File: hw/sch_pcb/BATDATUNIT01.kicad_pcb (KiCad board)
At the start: 2 copper layers, 136.2 x 85.9 mm, 222 parts, among them J1 USBC_USB4105-GF-A, J2 SD_Card-FPS009-4200-0, J3 HEADER_2x03, J4 46436-9327, Q1 BC817-25, Q2 BC817-25, Q3 BC817-25, Q4 BC817-25, Q5 BC817-25, Q6 BC817-25, Q7 BSS83P, SW1 SKRTLAE010, SW2 KMT031, SW3 SKRTLAE010, SW4 KMT031, U1 MAX14502AETL+, U10 PCF85263A, U11 TCA4307, U12 BQ34Z100, U13 BQ25628E, U14 SN74HC164P, U15 TPS631000DRLR, U16 TPS631000DRLR, U17 TPS631000DRLR, U18 TPS22965-Q1, U2 USBLC6-2SC6, U4 PCA9541ABS/01, U5 AT24CS64-SSHM, U6 SHT35-DIS, U7 TMUX1574DYYR, U8 ATMEGA1284P-AU, U9 MS561101BA03-50, Y1 19.2 MHz, Y2 8 MHz, Y3 ABS07-120-32.768KHZ-T

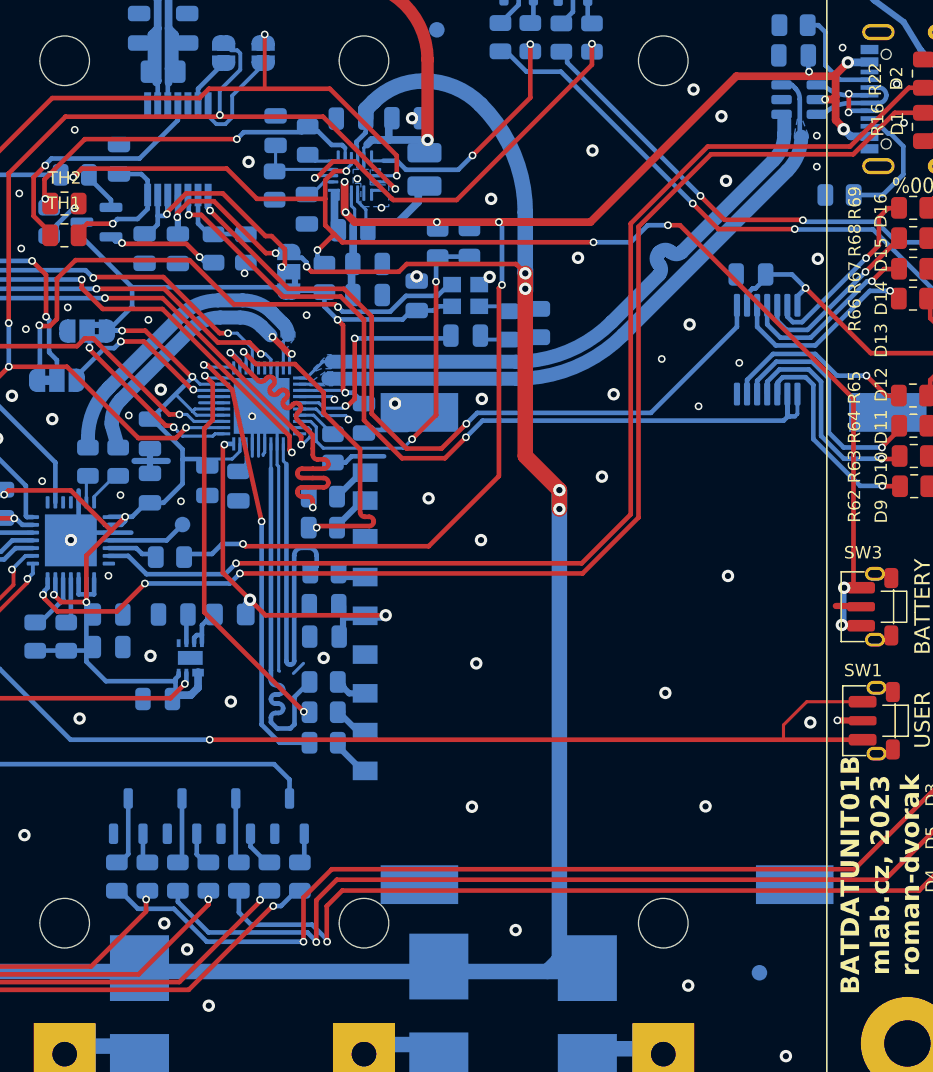
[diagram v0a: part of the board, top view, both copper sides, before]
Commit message: Move SD card reader  oscillator away from USB data tracks and isolate it by GND strip.
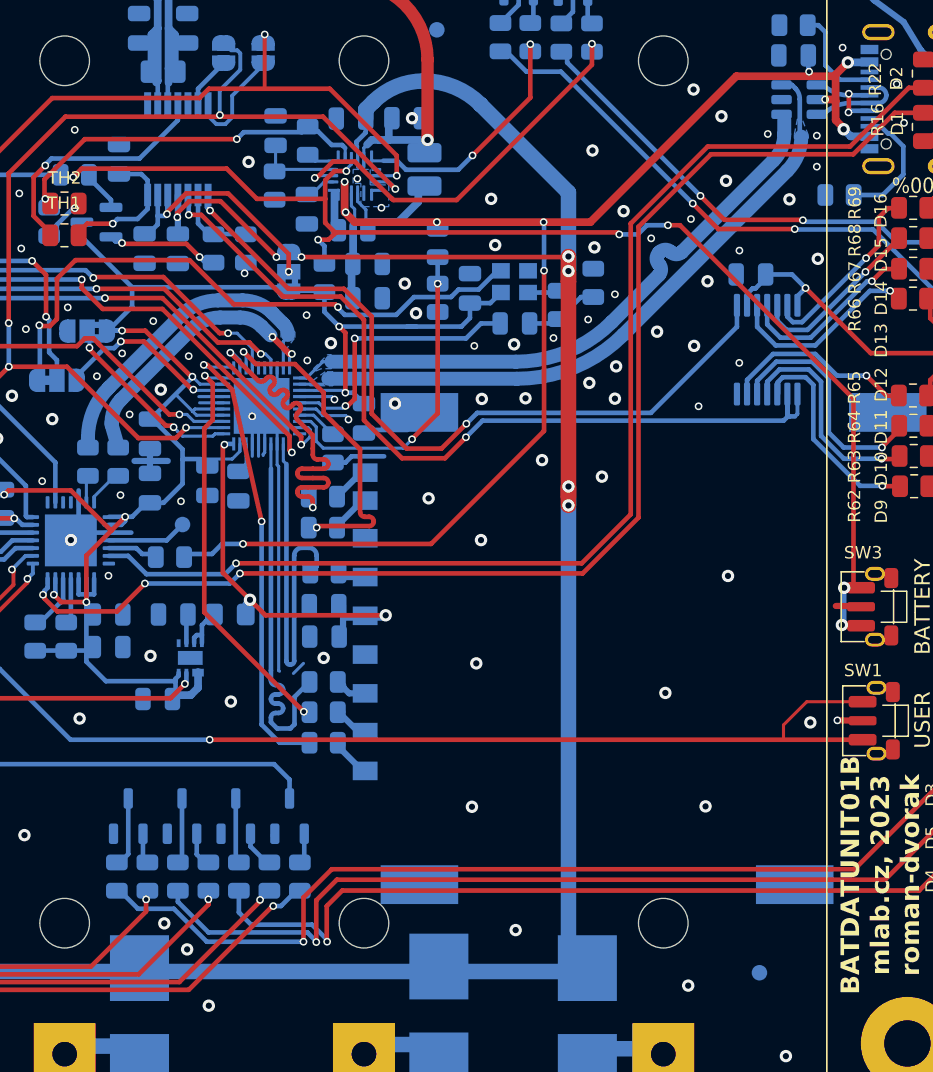
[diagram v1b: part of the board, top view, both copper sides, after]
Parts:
- moved R4 4.34 mm to (194.3, 91.5)
- moved R14 4.11 mm to (184.3, 92.5), turned to -90 degrees
- moved R3 3.49 mm to (192.0, 92.9)
- moved C4 3.47 mm to (186.3, 91.9)
- moved Y1 3.27 mm to (189.2, 91.4)
- moved C49 3.27 mm to (189.2, 94.1)
- moved C23 0.21 mm to (179.7, 92.5)
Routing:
- net +3.3V: track 564.6 -> 569.3 mm
- net /FREF: track 14.1 -> 17.6 mm
- net /mode_osc: track 36.1 -> 39.4 mm
- net +BATT: track 242.6 -> 245.4 mm
- net Net-(U1-KVBUS): track 23.2 -> 21.2 mm
- net VBUS: track 91.5 -> 90.1 mm
- net Net-(C49-Pad1): track 3.97 -> 4.81 mm
- net GND: vias 169 -> 191

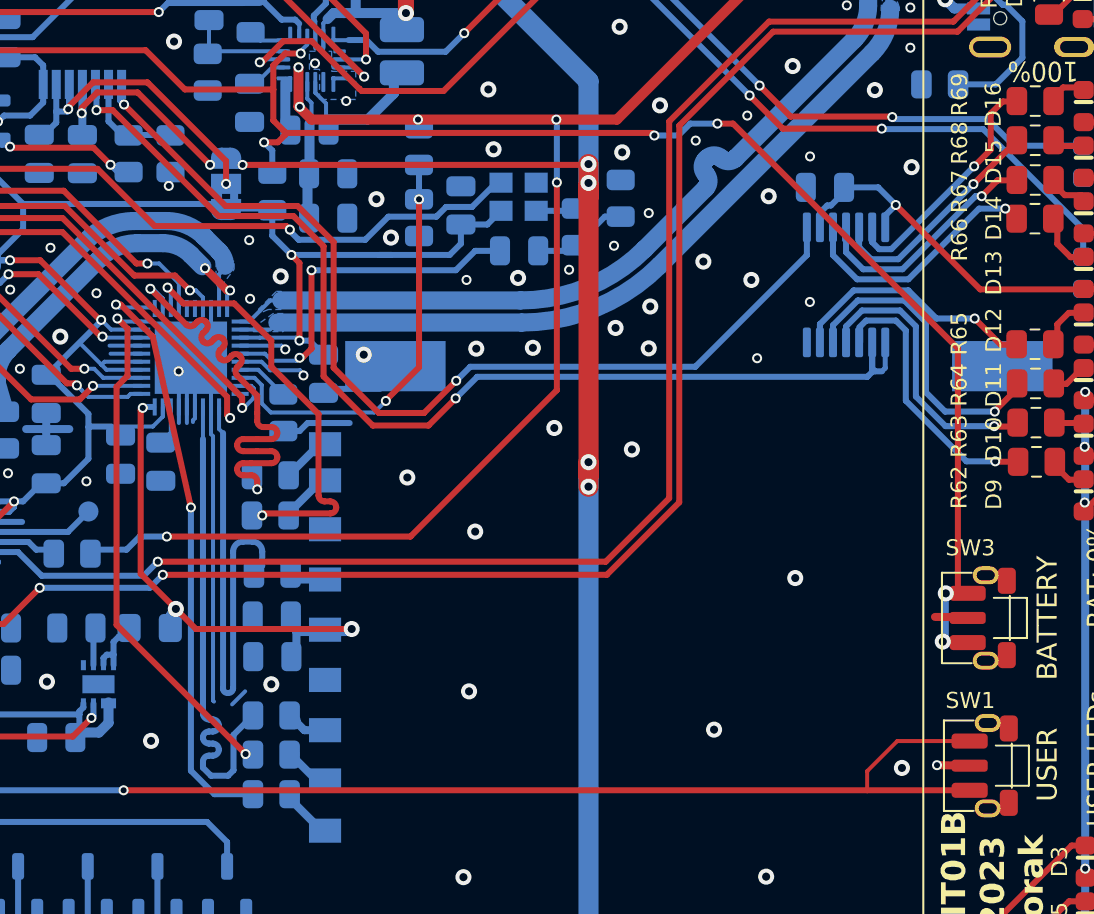
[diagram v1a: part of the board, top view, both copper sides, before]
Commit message: Swap button pins. Resolve #7
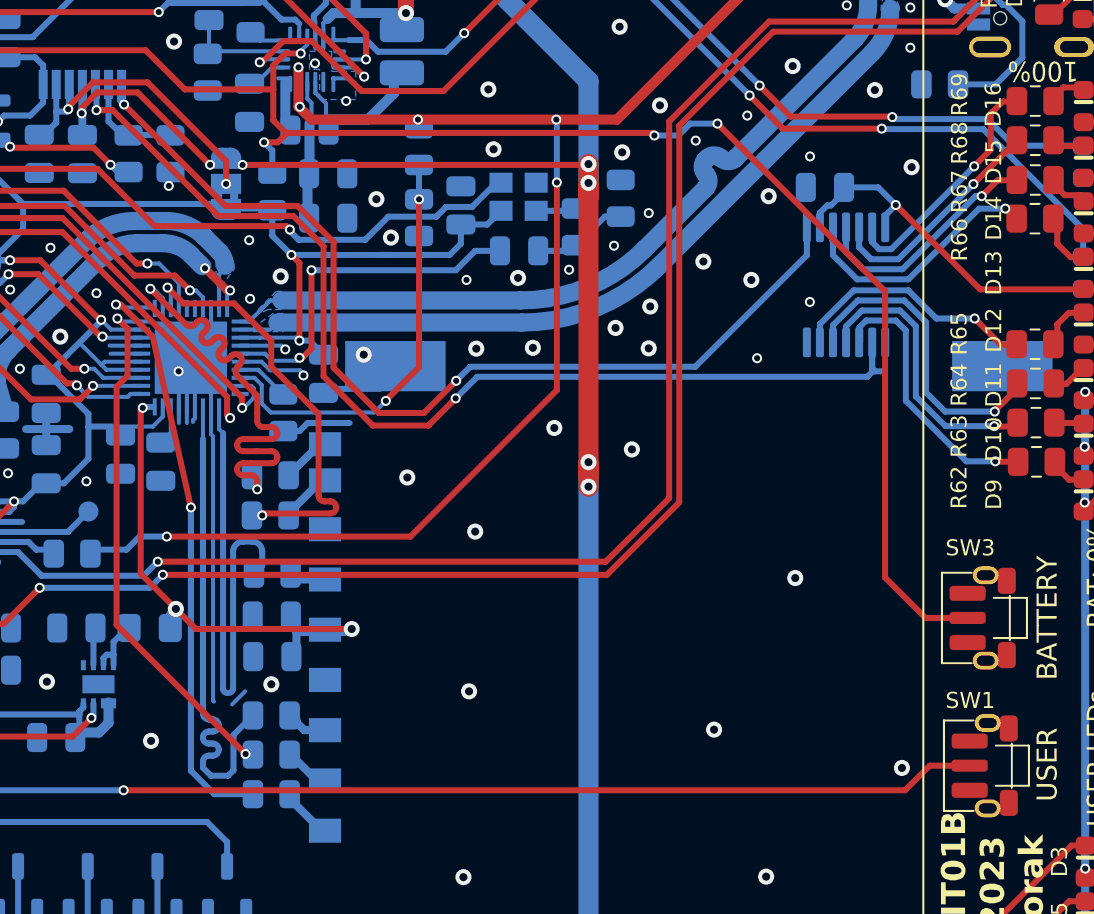
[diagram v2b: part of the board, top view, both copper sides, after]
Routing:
- net /BTN_USER_A: track 119.1 -> 113.0 mm
- net GND: track 94.3 -> 91.1 mm, vias 191 -> 190
- net EXT_DETECTION_CHARGER: track 178.4 -> 176.1 mm, vias 9 -> 7
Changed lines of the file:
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@@
     (fp_line (start 2.25 -1.28) (end 2.25 0.2)
       (stroke (width 0.1) (type default)) (layer "F.SilkS"))
-    (pad "1" smd roundrect (at -1.225 0 90) (size 0.75 1.8) (layers "F.Cu" "F.Paste" "F.Mask") (roundrect_rratio 0.25)
+    (pad "1" smd roundrect (at 0 0 90) (size 0.6 1.8) (layers "F.Cu" "F.Paste" "F.Mask") (roundrect_rratio 0.25)
       (net 210 "EXT_DETECTION_CHARGER") (pinfunction "1") (pintype "passive") (thermal_bridge_angle 45))
-    (pad "1" smd roundrect (at 1.225 0 90) (size 0.75 1.8) (layers "F.Cu" "F.Paste" "F.Mask") (roundrect_rratio 0.25)
-      (net 210 "EXT_DETECTION_CHARGER") (pinfunction "1") (pintype "passive") (thermal_bridge_angle 45))
-    (pad "2" smd roundrect (at 0 0 90) (size 0.6 1.8) (layers "F.Cu" "F.Paste" "F.Mask") (roundrect_rratio 0.25)
+    (pad "2" smd roundrect (at -1.225 0 90) (size 0.75 1.8) (layers "F.Cu" "F.Paste" "F.Mask") (roundrect_rratio 0.25)
+      (net 1 "GND") (pinfunction "2") (pintype "passive") (thermal_bridge_angle 45))
+    (pad "2" smd roundrect (at 1.225 0 90) (size 0.75 1.8) (layers "F.Cu" "F.Paste" "F.Mask") (roundrect_rratio 0.25)
       (net 1 "GND") (pinfunction "2") (pintype "passive") (thermal_bridge_angle 45))
     (pad "GND" thru_hole oval (at -2.125 0.9 90) (size 0.9 1.3) (drill oval 0.5 0.9) (layers "*.Cu" "*.Mask")
@@
     (fp_line (start 2.25 -1.28) (end 2.25 0.2)
       (stroke (width 0.1) (type default)) (layer "F.SilkS"))
-    (pad "1" smd roundrect (at -1.225 0 90) (size 0.75 1.8) (layers "F.Cu" "F.Paste" "F.Mask") (roundrect_rratio 0.25)
+    (pad "1" smd roundrect (at 0 0 90) (size 0.6 1.8) (layers "F.Cu" "F.Paste" "F.Mask") (roundrect_rratio 0.25)
       (net 43 "/BTN_USER_A") (pinfunction "1") (pintype "passive") (thermal_bridge_angle 45))
-    (pad "1" smd roundrect (at 1.225 0 90) (size 0.75 1.8) (layers "F.Cu" "F.Paste" "F.Mask") (roundrect_rratio 0.25)
-      (net 43 "/BTN_USER_A") (pinfunction "1") (pintype "passive") (thermal_bridge_angle 45))
-    (pad "2" smd roundrect (at 0 0 90) (size 0.6 1.8) (layers "F.Cu" "F.Paste" "F.Mask") (roundrect_rratio 0.25)
+    (pad "2" smd roundrect (at -1.225 0 90) (size 0.75 1.8) (layers "F.Cu" "F.Paste" "F.Mask") (roundrect_rratio 0.25)
+      (net 1 "GND") (pinfunction "2") (pintype "passive") (thermal_bridge_angle 45))
+    (pad "2" smd roundrect (at 1.225 0 90) (size 0.75 1.8) (layers "F.Cu" "F.Paste" "F.Mask") (roundrect_rratio 0.25)
       (net 1 "GND") (pinfunction "2") (pintype "passive") (thermal_bridge_angle 45))
     (pad "GND" thru_hole oval (at -2.125 0.9 90) (size 0.9 1.3) (drill oval 0.5 0.9) (layers "*.Cu" "*.Mask")
@@
     (style (thickness 0.15) (arrow_length 1.27) (text_position_mode 0) (extension_height 0.58642) (extension_offset 0.5) keep_text_aligned)
   )
-  (segment (start 210.025 119.725) (end 210.05 119.75) (width 0.4) (layer "F.Cu") (net 1))
+  (segment (start 211.516 113.576) (end 211.565 113.625) (width 0.3) (layer "F.Cu") (net 1))
   (segment (start 98.15 102) (end 95 102) (width 0.4) (layer "F.Cu") (net 1))
-  (segment (start 211.65 119.75) (end 210.025 119.725) (width 0.4) (layer "F.Cu") (net 1))
-  (segment (start 211.515 112.35) (end 209.925 112.35) (width 0.4) (layer "F.Cu") (net 1))
   (via (at 144.4498 73.4822) (size 0.8) (drill 0.4) (layers "F.Cu" "B.Cu") (free) (net 1))
   (via (at 141.859 78.1558) (size 0.8) (drill 0.4) (layers "F.Cu" "B.Cu") (free) (net 1))
@@
   (via (at 201.6506 91.4146) (size 0.8) (drill 0.4) (layers "F.Cu" "B.Cu") (free) (net 1))
   (via (at 143.2052 79.2988) (size 0.8) (drill 0.4) (layers "F.Cu" "B.Cu") (free) (net 1))
-  (via (at 210.025 119.725) (size 0.5) (drill 0.3) (layers "F.Cu" "B.Cu") (net 1))
   (via (at 115.25 96) (size 0.5) (drill 0.3) (layers "F.Cu" "B.Cu") (free) (net 1))
   (via (at 169.4942 138.1252) (size 0.8) (drill 0.4) (layers "F.Cu" "B.Cu") (free) (net 1))
@@
   (segment (start 112.35 77.62) (end 112.55 77.62) (width 0.3) (layer "B.Cu") (net 42))
   (segment (start 117.563589 98.511411) (end 117.563589 99.456411) (width 0.3) (layer "B.Cu") (net 42))
-  (segment (start 211.65 118.525) (end 208.05 118.525) (width 0.2) (layer "F.Cu") (net 43))
+  (segment (start 211.65 119.75) (end 209.6626 119.75) (width 0.3) (layer "F.Cu") (net 43))
   (segment (start 116.6 104.9) (end 116.6 105.6) (width 0.3) (layer "F.Cu") (net 43))
-  (segment (start 211.65 120.975) (end 206.55 120.975) (width 0.3) (layer "F.Cu") (net 43))
   (segment (start 125.348529 108.5) (end 133.248529 116.4) (width 0.3) (layer "F.Cu") (net 43))
-  (segment (start 206.55 120.975) (end 169.55 120.975) (width 0.3) (layer "F.Cu") (net 43))
+  (segment (start 209.6626 119.75) (end 208.4376 120.975) (width 0.3) (layer "F.Cu") (net 43))
   (segment (start 119.5 108.5) (end 125.348529 108.5) (width 0.3) (layer "F.Cu") (net 43))
   (segment (start 116.6 105.6) (end 119.5 108.5) (width 0.3) (layer "F.Cu") (net 43))
-  (segment (start 206.55 120.025) (end 206.55 120.975) (width 0.2) (layer "F.Cu") (net 43))
   (segment (start 133.248529 116.4) (end 143.9 116.4) (width 0.3) (layer "F.Cu") (net 43))
-  (segment (start 208.05 118.525) (end 206.55 120.025) (width 0.2) (layer "F.Cu") (net 43))
+  (segment (start 208.4376 120.975) (end 169.55 120.975) (width 0.3) (layer "F.Cu") (net 43))
   (via (at 143.9 116.4) (size 0.5) (drill 0.3) (layers "F.Cu" "B.Cu") (net 43))
   (via (at 169.55 120.975) (size 0.5) (drill 0.3) (layers "F.Cu" "B.Cu") (net 43))
@@
   (segment (start 118.419341 124.312893) (end 117.666117 125.066117) (width 0.25) (layer "B.Cu") (net 207))
   (arc (start 119.126448 124.02) (mid 118.743765 124.09612) (end 118.419341 124.312893) (width 0.25) (layer "B.Cu") (net 207))
-  (segment (start 210.465 111.175) (end 210.464 111.176) (width 0.3) (layer "F.Cu") (net 210))
+  (segment (start 207.4418 96.1418) (end 207.4418 110.3884) (width 0.3) (layer "F.Cu") (net 210))
   (segment (start 195.834 88.265) (end 195.961 88.392) (width 0.3) (layer "F.Cu") (net 210))
   (segment (start 146.3 119.9) (end 146.3 112.9) (width 0.3) (layer "F.Cu") (net 210))
   (segment (start 146.3 112.9) (end 142.9 109.5) (width 0.3) (layer "F.Cu") (net 210))
   (segment (start 160.75 84.7) (end 161.3 84.15) (width 0.3) (layer "F.Cu") (net 210))
-  (segment (start 211.516 113.576) (end 211.565 113.625) (width 0.3) (layer "F.Cu") (net 210))
-  (segment (start 211.064 98.989) (end 211.064 110.926) (width 0.3) (layer "F.Cu") (net 210))
   (segment (start 177 87.6428) (end 177 86.1) (width 0.3) (layer "F.Cu") (net 210))
   (segment (start 177.575 88.375) (end 177.2182 88.7318) (width 0.3) (layer "F.Cu") (net 210))
   (segment (start 177.685 88.265) (end 195.834 88.265) (width 0.3) (layer "F.Cu") (net 210))
   (segment (start 177 84.9) (end 177 86.1) (width 0.3) (layer "F.Cu") (net 210))
-  (segment (start 210.314 113.576) (end 211.516 113.576) (width 0.3) (layer "F.Cu") (net 210))
+  (segment (start 207.4418 110.3884) (end 209.4534 112.4) (width 0.3) (layer "F.Cu") (net 210))
+  (segment (start 199.1 87.8) (end 207.4418 96.1418) (width 0.3) (layer "F.Cu") (net 210))
   (segment (start 177.589471 84.310529) (end 177 84.9) (width 0.3) (layer "F.Cu") (net 210))
   (segment (start 142.9 109.5) (end 142.9 102.848529) (width 0.3) (layer "F.Cu") (net 210))
-  (segment (start 199.1 87.8) (end 199.875 87.8) (width 0.3) (layer "F.Cu") (net 210))
   (segment (start 178.364466 84.310529) (end 177.589471 84.310529) (width 0.3) (layer "F.Cu") (net 210))
   (segment (start 161.3 84.15) (end 170.65 84.15) (width 0.3) (layer "F.Cu") (net 210))
@@
   (segment (start 177.2182 88.7318) (end 176.541565 88.7318) (width 0.3) (layer "F.Cu") (net 210))
   (segment (start 170.65 84.15) (end 172.6 86.1) (width 0.3) (layer "F.Cu") (net 210))
-  (segment (start 199.875 87.8) (end 211.064 98.989) (width 0.3) (layer "F.Cu") (net 210))
-  (segment (start 211.565 111.175) (end 210.465 111.175) (width 0.3) (layer "F.Cu") (net 210))
+  (segment (start 209.4534 112.4) (end 211.55 112.4) (width 0.3) (layer "F.Cu") (net 210))
   (segment (start 177.575 88.375) (end 177.575 88.2178) (width 0.3) (layer "F.Cu") (net 210))
   (segment (start 172.6 86.1) (end 177 86.1) (width 0.3) (layer "F.Cu") (net 210))
@@
   (via (at 178.364466 84.310529) (size 0.5) (drill 0.3) (layers "F.Cu" "B.Cu") (net 210))
   (via (at 195.961 88.392) (size 0.5) (drill 0.3) (layers "F.Cu" "B.Cu") (net 210))
-  (via (at 210.464 111.176) (size 0.8) (drill 0.4) (layers "F.Cu" "B.Cu") (net 210))
   (via (at 199.1 87.8) (size 0.5) (drill 0.3) (layers "F.Cu" "B.Cu") (net 210))
-  (via (at 210.314 113.576) (size 0.8) (drill 0.4) (layers "F.Cu" "B.Cu") (net 210))
   (via (at 153.299996 84.55) (size 0.5) (drill 0.3) (layers "F.Cu" "B.Cu") (net 210))
   (segment (start 197.7468 87.8) (end 197.1548 88.392) (width 0.3) (layer "B.Cu") (net 210))
@@
   (segment (start 153.3 84.55) (end 153.299996 84.55) (width 0.3) (layer "B.Cu") (net 210))
   (segment (start 140.5 125.7) (end 146.3 119.9) (width 0.3) (layer "B.Cu") (net 210))
-  (segment (start 210.464 111.176) (end 210.464 113.426) (width 0.3) (layer "B.Cu") (net 210))
   (segment (start 116.6 87.41) (end 116.6 85.4375) (width 0.3) (layer "B.Cu") (net 210))
   (segment (start 197.1548 88.392) (end 195.961 88.392) (width 0.3) (layer "B.Cu") (net 210))
@@
   (segment (start 176.95 89.140235) (end 176.541565 88.7318) (width 0.3) (layer "B.Cu") (net 210))
   (segment (start 116.6 87.41) (end 117.06 86.95) (width 0.3) (layer "B.Cu") (net 210))
-  (segment (start 210.464 113.426) (end 210.314 113.576) (width 0.3) (layer "B.Cu") (net 210))
   (segment (start 148.1 84.55) (end 153.3 84.55) (width 0.3) (layer "B.Cu") (net 210))
   (segment (start 178.364466 84.310529) (end 178.364466 84.191219) (width 0.2) (layer "B.Cu") (net 210))
